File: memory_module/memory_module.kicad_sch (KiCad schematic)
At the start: 82 parts, among them SW1 SW_DIP_x08, SW2 SW_DIP_x08, SW3 SW_DIP_x08, SW4 SW_DIP_x08, SW5 SW_DIP_x08, SW6 SW_DIP_x08, SW7 SW_DIP_x08, SW8 SW_DIP_x08, U1 74HC138, U3 74LS540

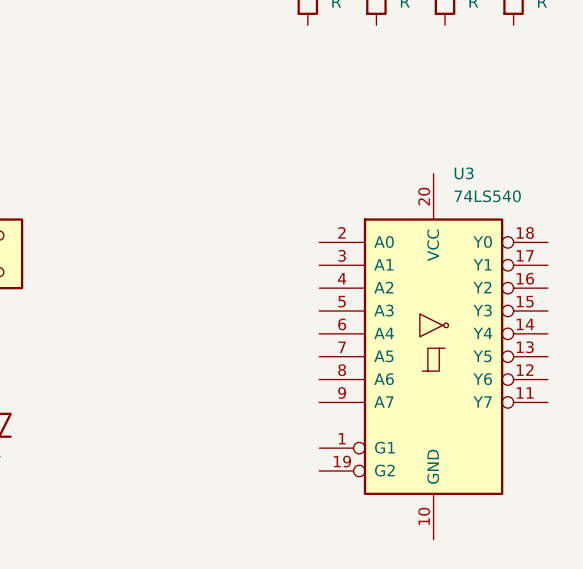
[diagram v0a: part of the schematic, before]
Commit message: ICのフットプリントを追加
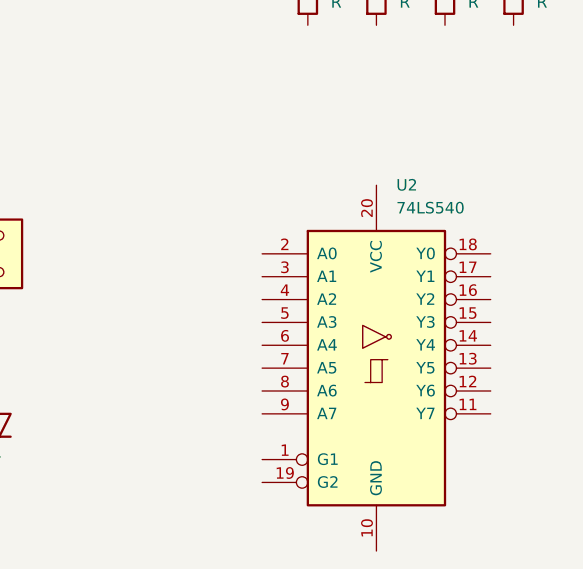
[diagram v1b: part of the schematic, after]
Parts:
- removed U3: 74LS540, symbol 74xx:74LS540
- added U2: 74LS540, TD4_footprint:DIP20_TOS, symbol 74xx:74LS540
- U1: footprint (none) -> TD4_footprint:DIP16
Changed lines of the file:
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@@
-	)
-	(symbol
-		(lib_id "74xx:74LS540")
-		(at 257.81 120.65 0)
-		(unit 1)
-		(exclude_from_sim no)
-		(in_bom yes)
-		(on_board yes)
-		(dnp no)
-		(fields_autoplaced yes)
-		(property "Reference" "U3"
-			(at 260.0041 100.33 0)
-			(effects
-				(font
-					(size 1.27 1.27)
-				)
-				(justify left)
-			)
-		)
-		(property "Value" "74LS540"
-			(at 260.0041 102.87 0)
-			(effects
-				(font
-					(size 1.27 1.27)
-				)
-				(justify left)
-			)
-		)
-		(property "Footprint" ""
-			(at 257.81 120.65 0)
-			(effects
-				(font
-					(size 1.27 1.27)
-				)
-				(hide yes)
-			)
-		)
-		(property "Datasheet" "http://www.ti.com/lit/gpn/sn74LS540"
-			(at 257.81 120.65 0)
-			(effects
-				(font
-					(size 1.27 1.27)
-				)
-				(hide yes)
-			)
-		)
-		(property "Description" "8-bit Buffer/Line driver Inverter, 3-state outputs"
-			(at 257.81 120.65 0)
-			(effects
-				(font
-					(size 1.27 1.27)
-				)
-				(hide yes)
-			)
-		)
-		(pin "10"
-		)
-		(pin "3"
-		)
-		(pin "8"
-		)
-		(pin "18"
-		)
-		(pin "9"
-		)
-		(pin "15"
-		)
-		(pin "11"
-		)
-		(pin "19"
-		)
-		(pin "2"
-		)
-		(pin "7"
-		)
-		(pin "14"
-		)
-		(pin "16"
-		)
-		(pin "20"
-		)
-		(pin "6"
-		)
-		(pin "4"
-		)
-		(pin "1"
-		)
-		(pin "13"
-		)
-		(pin "12"
-		)
-		(pin "17"
-		)
-		(pin "5"
-		)
-		(instances
-			(project ""
-				(path "/cb456c8d-c165-427f-90fc-43ce7c6cbf26"
-					(reference "U3")
-					(unit 1)
-				)
-			)
-		)
 	)
 	(symbol
@@
 				(path "/cb456c8d-c165-427f-90fc-43ce7c6cbf26"
 					(reference "SW3")
+					(unit 1)
+				)
+			)
+		)
+	)
+	(symbol
+		(lib_id "74xx:74LS540")
+		(at 251.46 121.92 0)
+		(unit 1)
+		(exclude_from_sim no)
+		(in_bom yes)
+		(on_board yes)
+		(dnp no)
+		(fields_autoplaced yes)
+		(property "Reference" "U2"
+			(at 253.6541 101.6 0)
+			(effects
+				(font
+					(size 1.27 1.27)
+				)
+				(justify left)
+			)
+		)
+		(property "Value" "74LS540"
+			(at 253.6541 104.14 0)
+			(effects
+				(font
+					(size 1.27 1.27)
+				)
+				(justify left)
+			)
+		)
+		(property "Footprint" "TD4_footprint:DIP20_TOS"
+			(at 251.46 121.92 0)
+			(effects
+				(font
+					(size 1.27 1.27)
+				)
+				(hide yes)
+			)
+		)
+		(property "Datasheet" "http://www.ti.com/lit/gpn/sn74LS540"
+			(at 251.46 121.92 0)
+			(effects
+				(font
+					(size 1.27 1.27)
+				)
+				(hide yes)
+			)
+		)
+		(property "Description" "8-bit Buffer/Line driver Inverter, 3-state outputs"
+			(at 251.46 121.92 0)
+			(effects
+				(font
+					(size 1.27 1.27)
+				)
+				(hide yes)
+			)
+		)
+		(pin "10"
+		)
+		(pin "11"
+		)
+		(pin "6"
+		)
+		(pin "4"
+		)
+		(pin "1"
+		)
+		(pin "3"
+		)
+		(pin "5"
+		)
+		(pin "15"
+		)
+		(pin "20"
+		)
+		(pin "17"
+		)
+		(pin "8"
+		)
+		(pin "19"
+		)
+		(pin "9"
+		)
+		(pin "12"
+		)
+		(pin "18"
+		)
+		(pin "16"
+		)
+		(pin "2"
+		)
+		(pin "7"
+		)
+		(pin "13"
+		)
+		(pin "14"
+		)
+		(instances
+			(project ""
+				(path "/cb456c8d-c165-427f-90fc-43ce7c6cbf26"
+					(reference "U2")
 					(unit 1)
 				)
@@
 			)
 		)
-		(property "Footprint" ""
+		(property "Footprint" "TD4_footprint:DIP16"
 			(at 41.91 128.27 0)
 			(effects

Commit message: 回路図進めた
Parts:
- added D65, D66, D67, D68, D69, D70, D71, D72: LED, LED_THT:LED_D3.0mm, symbol Device:LED
- added R9: R, Resistor_THT:R_Axial_DIN0207_L6.3mm_D2.5mm_P10.16mm_Horizontal, symbol Device:R
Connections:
- net at R1.1: now also SW1.16, SW2.16, SW3.16, SW4.16, SW5.16, SW6.16, SW7.16, SW8.16, U2.9 (A7)
- net +5V: now reaches R1.2
- net +5V: now also R2.2, R3.2, R4.2, R5.2, R6.2, R7.2, R8.2, U1.16 (VCC), U1.4 (~{E0}), R9.1
- net at D13.1 (K): now also D10.1 (K), D11.1 (K), D12.1 (K), D14.1 (K), D15.1 (K), D16.1 (K), D9.1 (K), U1.14 (~{Y1}), D66.1 (K)
- net at D56.1 (K): now also D49.1 (K), D50.1 (K), D51.1 (K), D52.1 (K), D53.1 (K), D54.1 (K), D55.1 (K), U1.9 (~{Y6}), D71.1 (K)
- net at D27.1 (K): now also D25.1 (K), D26.1 (K), D28.1 (K), D29.1 (K), D30.1 (K), D31.1 (K), D32.1 (K), U1.12 (~{Y3}), D68.1 (K)
- net at R4.1: now also SW1.13, SW2.13, SW3.13, SW4.13, SW5.13, SW6.13, SW7.13, SW8.13, U2.6 (A4)
- net at D17.1 (K): now also D18.1 (K), D19.1 (K), D20.1 (K), D21.1 (K), D22.1 (K), D23.1 (K), D24.1 (K), U1.13 (~{Y2}), D67.1 (K)
- net at D7.1 (K): now also D1.1 (K), D2.1 (K), D3.1 (K), D4.1 (K), D5.1 (K), D6.1 (K), D8.1 (K), U1.15 (~{Y0}), D65.1 (K)
- net at D62.1 (K): now also D57.1 (K), D58.1 (K), D59.1 (K), D60.1 (K), D61.1 (K), D63.1 (K), D64.1 (K), U1.7 (~{Y7}), D72.1 (K)
- net at R3.1: now also SW1.14, SW2.14, SW3.14, SW4.14, SW5.14, SW6.14, SW7.14, SW8.14, U2.7 (A5)
- net at D40.1 (K): now also D33.1 (K), D34.1 (K), D35.1 (K), D36.1 (K), D37.1 (K), D38.1 (K), D39.1 (K), U1.11 (~{Y4}), D69.1 (K)
- net at R5.1: now also SW1.12, SW2.12, SW3.12, SW4.12, SW5.12, SW6.12, SW7.12, SW8.12, U2.5 (A3)
- net at D41.1 (K): now also D42.1 (K), D43.1 (K), D44.1 (K), D45.1 (K), D46.1 (K), D47.1 (K), D48.1 (K), U1.10 (~{Y5}), D70.1 (K)
- net at SW8.10: now also R7.1, SW1.10, SW2.10, SW3.10, SW4.10, SW5.10, SW6.10, SW7.10, U2.3 (A1)
- net at SW8.11: now also R6.1, SW1.11, SW2.11, SW3.11, SW4.11, SW5.11, SW6.11, SW7.11, U2.4 (A2)
- net at SW8.15: now also R2.1, SW1.15, SW2.15, SW3.15, SW4.15, SW5.15, SW6.15, SW7.15, U2.8 (A6)
- net at SW8.9: now also R8.1, SW1.9, SW2.9, SW3.9, SW4.9, SW5.9, SW6.9, SW7.9, U2.2 (A0)
- net GND: now reaches U2.1 (G1)
- net GND: now also U1.5 (~{E1}), U1.6 (E2), U1.8 (GND), U2.10 (GND), U2.19 (G2)
- net D7: now reaches U2.11 (Y7)
- net D6: now reaches U2.12 (Y6)
- net D5: now reaches U2.13 (Y5)
- net D4: now reaches U2.14 (Y4)
- net D3: now reaches U2.15 (Y3)
- net D2: now reaches U2.16 (Y2)
- net D1: now reaches U2.17 (Y1)
- net D0: now reaches U2.18 (Y0)
- net A0: now reaches U1.1 (A0)
- net A1: now reaches U1.2 (A1)
- net A2: now reaches U1.3 (A2)
- new net: D65.2 (A), D66.2 (A), D67.2 (A), D68.2 (A), D69.2 (A), D70.2 (A), D71.2 (A), D72.2 (A), R9.2
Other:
- moved on the sheet: D1, D10, D11, D12, D13, D14, D15, D16, D17, D18, D19, D2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

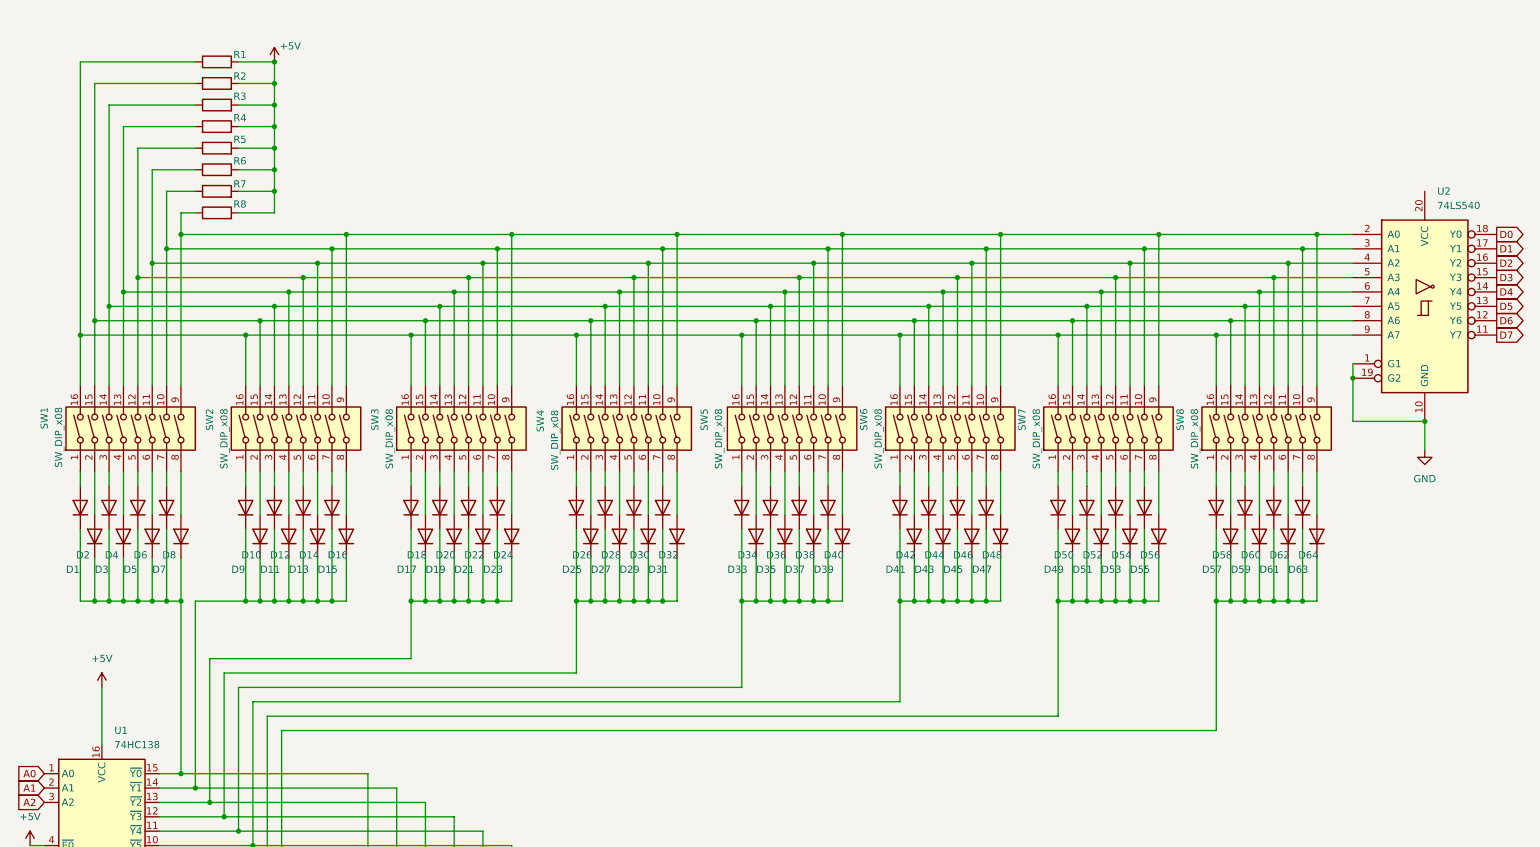
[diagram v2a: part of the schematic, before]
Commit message: 回路図にコネクターを追加
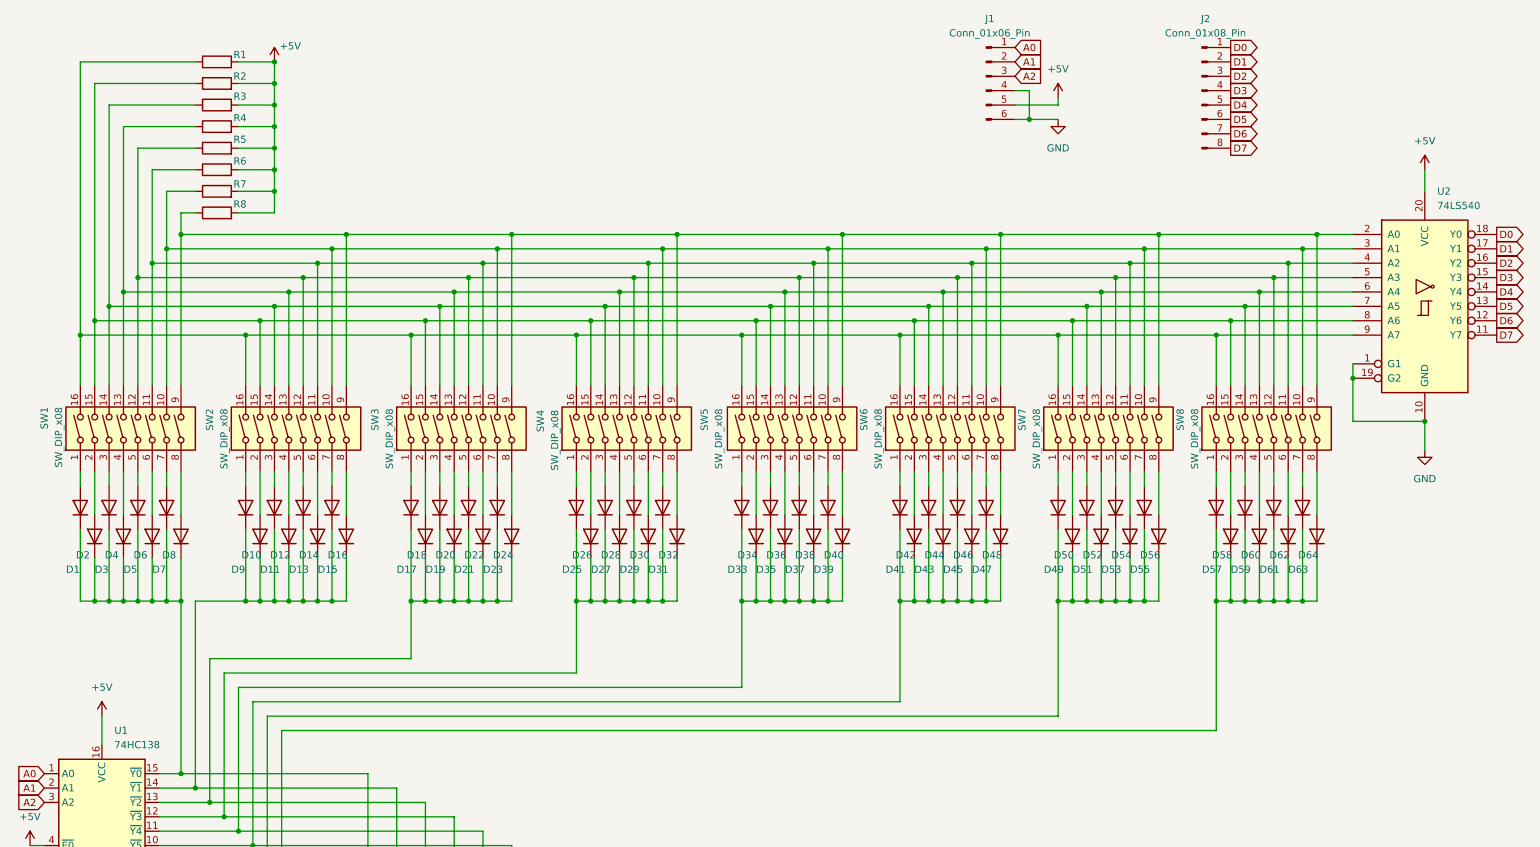
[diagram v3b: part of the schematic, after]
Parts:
- added J1: Conn_01x06_Pin, symbol Connector:Conn_01x06_Pin
- added J2: Conn_01x08_Pin, symbol Connector:Conn_01x08_Pin
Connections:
- net +5V: now also U2.20 (VCC), J1.5 (Pin_5)
- net A0: now also J1.1 (Pin_1)
- net A1: now also J1.2 (Pin_2)
- net A2: now also J1.3 (Pin_3)
- net D0: now also J2.1 (Pin_1)
- net D1: now also J2.2 (Pin_2)
- net D2: now also J2.3 (Pin_3)
- net D3: now also J2.4 (Pin_4)
- net D4: now also J2.5 (Pin_5)
- net D5: now also J2.6 (Pin_6)
- net D6: now also J2.7 (Pin_7)
- net D7: now also J2.8 (Pin_8)
- net GND: now also J1.4 (Pin_4), J1.6 (Pin_6)
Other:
- title: (none) -> TD4 Memory Module

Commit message: ピンヘッダーにフットプリントを追加
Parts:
- J1: footprint (none) -> Connector_PinHeader_2.54mm:PinHeader_1x06_P2.54mm_Horizontal
- J2: footprint (none) -> Connector_PinHeader_2.54mm:PinHeader_1x08_P2.54mm_Horizontal
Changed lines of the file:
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@@
 			)
 		)
-		(property "Footprint" ""
+		(property "Footprint" "Connector_PinHeader_2.54mm:PinHeader_1x08_P2.54mm_Horizontal"
 			(at 223.52 36.83 0)
 			(effects
@@
 			)
 		)
-		(property "Footprint" ""
+		(property "Footprint" "Connector_PinHeader_2.54mm:PinHeader_1x06_P2.54mm_Horizontal"
 			(at 185.42 34.29 0)
 			(effects

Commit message: ガーバーファイル作成
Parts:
- U1: footprint TD4_footprint:DIP16 -> TD4_footprint:DIP16_TOS
- U2: value 74LS540 -> 74HC540
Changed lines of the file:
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@@
 			)
 		)
-		(property "Value" "74LS540"
+		(property "Value" "74HC540"
 			(at 265.0841 57.15 0)
 			(effects
@@
 			)
 		)
-		(property "Footprint" "TD4_footprint:DIP16"
+		(property "Footprint" "TD4_footprint:DIP16_TOS"
 			(at 29.21 167.64 0)
 			(effects

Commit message: wip
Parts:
- added D100, D101, D102, D103, D104, D105, D106, D107, D108, D109, D110, D111, D112, D113, D114, D115, D116, D117, D118, D119, D120, D121, D122, D123, D124, D125, D126, D127, D128, D65, D66, D67, D68, D69, D70, D71, D72, D73, D74, D75, D76, D77, D78, D79, D80, D81, D82, D83, D84, D85, D86, D87, D88, D89, D90, D91, D92, D93, D94, D95, D96, D97, D98, D99: 1N4148, Diode_THT:D_DO-35_SOD27_P2.54mm_Vertical_KathodeUp, symbol Diode:1N4148
- added D137, D138, D139, D140, D141, D142, D143, D144: LED, LED_THT:LED_D3.0mm, symbol Device:LED
- added SW10, SW11, SW12, SW13, SW14, SW15, SW16, SW9: SW_DIP_x08, Button_Switch_THT:SW_DIP_SPSTx08_Slide_9.78x22.5mm_W7.62mm_P2.54mm, symbol Switch:SW_DIP_x08
- added U2: 74HC138, TD4_footprint:DIP16_TOS, symbol 74xx:74HC138
- D1, D10, D11, D12, D13, D14, D15, D16, D17, D18, D19, D2, D20, D21, D22, D23, D24, D25, D26, D27, D28, D29, D3, D30, D31, D32, D33, D34, D35, D36, D37, D38, D39, D4, D40, D41, D42, D43, D44, D45, D46, D47, D48, D49, D5, D50, D51, D52, D53, D54, D55, D56, D57, D58, D59, D6, D60, D61, D62, D63, D64, D7, D8, D9: footprint Diode_THT:D_DO-35_SOD27_P7.62mm_Horizontal -> Diode_THT:D_DO-35_SOD27_P2.54mm_Vertical_KathodeUp
- renumbered D65 to D129, D66 to D130, D67 to D131, D68 to D132, D69 to D133, D70 to D134, D71 to D135, D72 to D136, U2 to U3
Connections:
- net +5V: now also U2.16 (VCC)
- net A0: now also U2.1 (A0)
- net A1: now also U2.2 (A1)
- net A2: now also U2.3 (A2)
- net GND: now also U2.5 (~{E1}), U2.6 (E2), U2.8 (GND); no longer J1.4 (Pin_4), U1.5 (~{E1}), U1.6 (E2)
- net at D129.2 (A), D130.2 (A), D131.2 (A)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: now also D137.2 (A), D138.2 (A), D139.2 (A), D140.2 (A), D141.2 (A), D142.2 (A), D143.2 (A), D144.2 (A)
- net at R1.1, SW1.16, SW2.16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: now also SW10.16, SW11.16, SW12.16, SW13.16, SW14.16, SW15.16, SW16.16, SW9.16
- net at R3.1, SW1.14, SW2.14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: now also SW10.14, SW11.14, SW12.14, SW13.14, SW14.14, SW15.14, SW16.14, SW9.14
- net at R6.1, SW1.11, SW2.11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: now also SW10.11, SW11.11, SW12.11, SW13.11, SW14.11, SW15.11, SW16.11, SW9.11
- net at R2.1, SW1.15, SW2.15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: now also SW10.15, SW11.15, SW12.15, SW13.15, SW14.15, SW15.15, SW16.15, SW9.15
- net at R7.1, SW1.10, SW2.10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: now also SW10.10, SW11.10, SW12.10, SW13.10, SW14.10, SW15.10, SW16.10, SW9.10
- net at R5.1, SW1.12, SW2.12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: now also SW10.12, SW11.12, SW12.12, SW13.12, SW14.12, SW15.12, SW16.12, SW9.12
- net at R4.1, SW1.13, SW2.13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: now also SW10.13, SW11.13, SW12.13, SW13.13, SW14.13, SW15.13, SW16.13, SW9.13
- net at R8.1, SW1.9, SW2.9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: now also SW10.9, SW11.9, SW12.9, SW13.9, SW14.9, SW15.9, SW16.9, SW9.9
- new net: D100.1 (K), D101.1 (K), D102.1 (K), D103.1 (K), D104.1 (K), D97.1 (K), D98.1 (K), D99.1 (K)
- new net: D98.2 (A), SW13.2
- new net: D121.2 (A), SW16.1
- new net: D122.2 (A), SW16.2
- new net: D123.2 (A), SW16.3
- new net: D124.2 (A), SW16.4
- new net: D125.2 (A), SW16.5
- new net: D126.2 (A), SW16.6
- new net: D127.2 (A), SW16.7
- new net: D128.2 (A), SW16.8
- new net: D73.1 (K), D74.1 (K), D75.1 (K), D76.1 (K), D77.1 (K), D78.1 (K), D79.1 (K), D80.1 (K)
- new net: D74.2 (A), SW10.2
- new net: D105.1 (K), D106.1 (K), D107.1 (K), D108.1 (K), D109.1 (K), D110.1 (K), D111.1 (K), D112.1 (K)
- new net: D112.2 (A), SW14.8
- new net: D78.2 (A), SW10.6
- new net: D65.2 (A), SW9.1
- new net: D66.2 (A), SW9.2
- new net: D67.2 (A), SW9.3
- new net: D68.2 (A), SW9.4
- new net: D69.2 (A), SW9.5
- new net: D70.2 (A), SW9.6
- new net: D71.2 (A), SW9.7
- new net: D72.2 (A), SW9.8
- new net: D65.1 (K), D66.1 (K), D67.1 (K), D68.1 (K), D69.1 (K), D70.1 (K), D71.1 (K), D72.1 (K)
- new net: D75.2 (A), SW10.3
- new net: D138.1 (K), U2.14 (~{Y1})
- new net: D121.1 (K), D122.1 (K), D123.1 (K), D124.1 (K), D125.1 (K), D126.1 (K), D127.1 (K), D128.1 (K)
- new net: D141.1 (K), U2.11 (~{Y4})
- new net: D73.2 (A), SW10.1
- new net: D113.1 (K), D114.1 (K), D115.1 (K), D116.1 (K), D117.1 (K), D118.1 (K), D119.1 (K), D120.1 (K)
- new net: D114.2 (A), SW15.2
- new net: D120.2 (A), SW15.8
- new net: D81.1 (K), D82.1 (K), D83.1 (K), D84.1 (K), D85.1 (K), D86.1 (K), D87.1 (K), D88.1 (K)
- new net: D85.2 (A), SW11.5
- new net: D101.2 (A), SW13.5
- new net: D84.2 (A), SW11.4
- new net: D89.1 (K), D90.1 (K), D91.1 (K), D92.1 (K), D93.1 (K), D94.1 (K), D95.1 (K), D96.1 (K)
- new net: D90.2 (A), SW12.2
- new net: D81.2 (A), SW11.1
- new net: D82.2 (A), SW11.2
- new net: D83.2 (A), SW11.3
- new net: D86.2 (A), SW11.6
- new net: D87.2 (A), SW11.7
- new net: D88.2 (A), SW11.8
- new net: D108.2 (A), SW14.4
- new net: D117.2 (A), SW15.5
- new net: D95.2 (A), SW12.7
- new net: D111.2 (A), SW14.7
- new net: D103.2 (A), SW13.7
- new net: D107.2 (A), SW14.3
- new net: D105.2 (A), SW14.1
- new net: D106.2 (A), SW14.2
- new net: D109.2 (A), SW14.5
- new net: D110.2 (A), SW14.6
- new net: D139.1 (K), U2.13 (~{Y2})
- new net: D91.2 (A), SW12.3
- new net: D119.2 (A), SW15.7
- new net: D77.2 (A), SW10.5
- new net: D93.2 (A), SW12.5
- new net: D97.2 (A), SW13.1
- new net: D99.2 (A), SW13.3
- new net: D100.2 (A), SW13.4
- new net: D102.2 (A), SW13.6
- new net: D104.2 (A), SW13.8
- new net: D137.1 (K), U2.15 (~{Y0})
- new net: D144.1 (K), U2.7 (~{Y7})
- new net: D115.2 (A), SW15.3
- new net: D89.2 (A), SW12.1
- new net: D92.2 (A), SW12.4
- new net: D94.2 (A), SW12.6
- new net: D96.2 (A), SW12.8
- new net: D142.1 (K), U2.10 (~{Y5})
- new net: D140.1 (K), U2.12 (~{Y3})
- new net: D143.1 (K), U2.9 (~{Y6})
- new net: D76.2 (A), SW10.4
- new net: D113.2 (A), SW15.1
- new net: D116.2 (A), SW15.4
- new net: D118.2 (A), SW15.6
- new net: D79.2 (A), SW10.7
- new net: D80.2 (A), SW10.8
- new net A3: J1.4 (Pin_4), U1.5 (~{E1}), U1.6 (E2), U2.4 (~{E0})
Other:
- moved on the sheet: D1, D10, D11, D12, D129, D13, D130, D131, D132, D133, D134, D135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

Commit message: wip
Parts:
- removed D129, D130, D131, D132, D133, D134, D135, D136, D137, D138, D139, D140, D141, D142, D143, D144: LED, LED_THT:LED_D3.0mm, symbol Device:LED
- removed R9: R, Resistor_THT:R_Axial_DIN0207_L6.3mm_D2.5mm_P10.16mm_Horizontal, symbol Device:R
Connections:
- net at D100.1 (K), D101.1 (K), D102.1 (K)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: now also U2.11 (~{Y4})
- net at D73.1 (K), D74.1 (K), D75.1 (K)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: now also U2.14 (~{Y1})
- net at D105.1 (K), D106.1 (K), D107.1 (K)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: now also U2.10 (~{Y5})
- net at D65.1 (K), D66.1 (K), D67.1 (K)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: now also U2.15 (~{Y0})
- net at D121.1 (K), D122.1 (K), D123.1 (K)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: now also U2.7 (~{Y7})
- net at D113.1 (K), D114.1 (K), D115.1 (K)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: now also U2.9 (~{Y6})
- net at D81.1 (K), D82.1 (K), D83.1 (K)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: now also U2.13 (~{Y2})
- net at D89.1 (K), D90.1 (K), D91.1 (K)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: now also U2.12 (~{Y3})

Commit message: とりあえず配線した、美しくはない
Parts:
- added D129, D130, D131, D132, D133, D134, D135, D136, D137, D138, D139, D140, D141, D142, D143, D144: LED, LED_SMD:LED_1206_3216Metric_Pad1.42x1.75mm_HandSolder, symbol Device:LED
- added R9: 1K, Resistor_THT:R_Axial_DIN0207_L6.3mm_D2.5mm_P2.54mm_Vertical, symbol Device:R
- R1, R2: value R -> 10K; footprint Resistor_THT:R_Axial_DIN0207_L6.3mm_D2.5mm_P10.16mm_Horizontal -> Resistor_THT:R_Axial_DIN0207_L6.3mm_D2.5mm_P2.54mm_Vertical
- R3, R4, R5, R6, R7, R8: footprint Resistor_THT:R_Axial_DIN0207_L6.3mm_D2.5mm_P10.16mm_Horizontal -> Resistor_THT:R_Axial_DIN0207_L6.3mm_D2.5mm_P2.54mm_Vertical
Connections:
- net +5V: now also R9.1
- net at D100.1 (K), D101.1 (K), D102.1 (K)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: now also D141.1 (K)
- net at D73.1 (K), D74.1 (K), D75.1 (K)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: now also D138.1 (K)
- net at D105.1 (K), D106.1 (K), D107.1 (K)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: now also D142.1 (K)
- net at D10.1 (K), D11.1 (K), D12.1 (K)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: now also D130.1 (K)
- net at D49.1 (K), D50.1 (K), D51.1 (K)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: now also D135.1 (K)
- net at D25.1 (K), D26.1 (K), D27.1 (K)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: now also D132.1 (K)
- net at D65.1 (K), D66.1 (K), D67.1 (K)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: now also D137.1 (K)
- net at D121.1 (K), D122.1 (K), D123.1 (K)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: now also D144.1 (K)
- net at D17.1 (K), D18.1 (K), D19.1 (K)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: now also D131.1 (K)
- net at D113.1 (K), D114.1 (K), D115.1 (K)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: now also D143.1 (K)
- net at D81.1 (K), D82.1 (K), D83.1 (K)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: now also D139.1 (K)
- net at D1.1 (K), D2.1 (K), D3.1 (K)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: now also D129.1 (K)
- net at D57.1 (K), D58.1 (K), D59.1 (K)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: now also D136.1 (K)
- net at D33.1 (K), D34.1 (K), D35.1 (K)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: now also D133.1 (K)
- net at D89.1 (K), D90.1 (K), D91.1 (K)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: now also D140.1 (K)
- net at D41.1 (K), D42.1 (K), D43.1 (K)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: now also D134.1 (K)
- new net: D129.2 (A), D130.2 (A), D131.2 (A), D132.2 (A), D133.2 (A), D134.2 (A), D135.2 (A), D136.2 (A), D137.2 (A), D138.2 (A), D139.2 (A), D140.2 (A), D141.2 (A), D142.2 (A), D143.2 (A), D144.2 (A), R9.2
